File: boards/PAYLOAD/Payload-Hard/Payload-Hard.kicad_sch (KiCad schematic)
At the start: 18 parts, among them J101 Micro_SD_Card, J102 Conn_01x05_Female, J103 Conn_01x07_Male, P101 S3B-PH-SM4-TB, U1 LM358, U102 3SP_SO2_20

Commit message: Yo
Yo
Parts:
- removed U1: LM358, Package_DIP:DIP-8_W10.16mm, symbol Amplifier_Operational:LM358
- added J104: Screw_Terminal_01x02, TerminalBlock_TE-Connectivity:TerminalBlock_TE_282834-2_1x02_P2.54mm_Horizontal, symbol Connector:Screw_Terminal_01x02
- added U101: OPAMP, symbol pspice:OPAMP
- added U103: Opamp_Dual, symbol Device:Opamp_Dual
- R108: value 10k -> R_US
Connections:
- net 3V3: now also U101.4 (V+)
- net Counter: now also U101.3
- net GND: now also J104.2 (Pin_2), U101.5 (V-)
- net Reference: now also U101.2 (-)
- net SO2_Out: now also U103.1
- net at R101.2, R102.1: now also U101.1 (+)
- net at C103.1, R106.2, R108.1: now also U103.2 (-)
- net at R105.2, R107.1: now also U103.3 (+)
- net Vbattery: now reaches A101.30 (VIN)
- net Vbattery: now also J104.1 (Pin_1)
- no-connect marks 19 -> 18
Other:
- note added: "Power Pins"

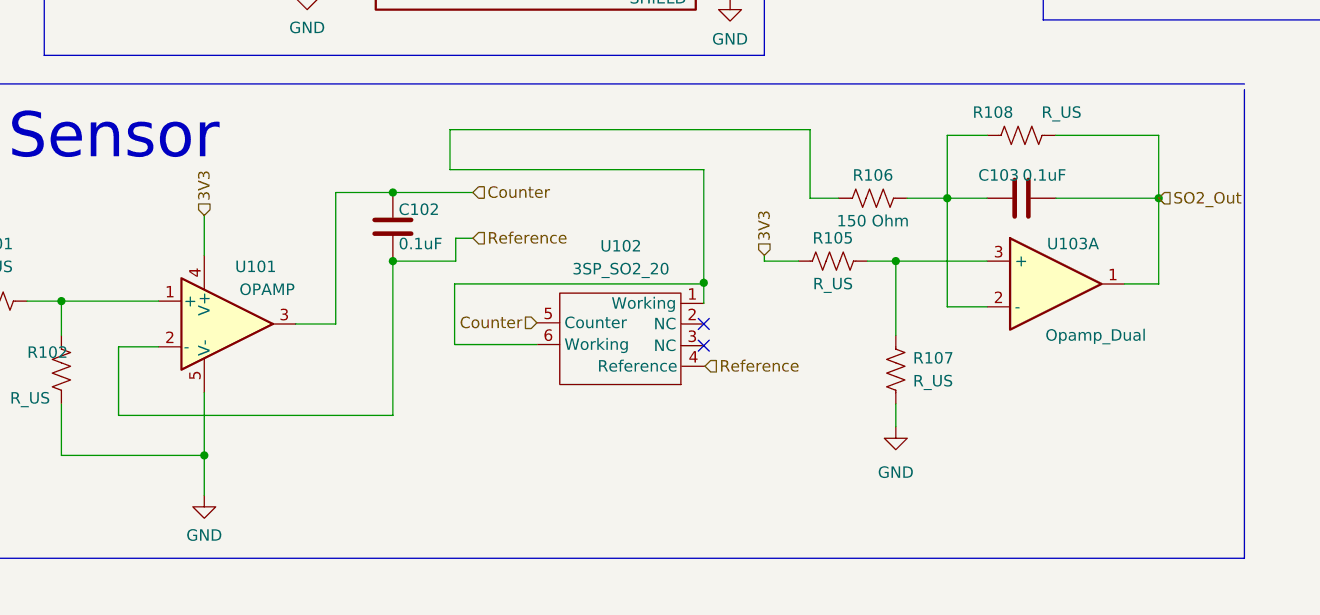
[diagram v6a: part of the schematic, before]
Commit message: CHanged OpAmp Symbol
CHanged OpAmp Symbol
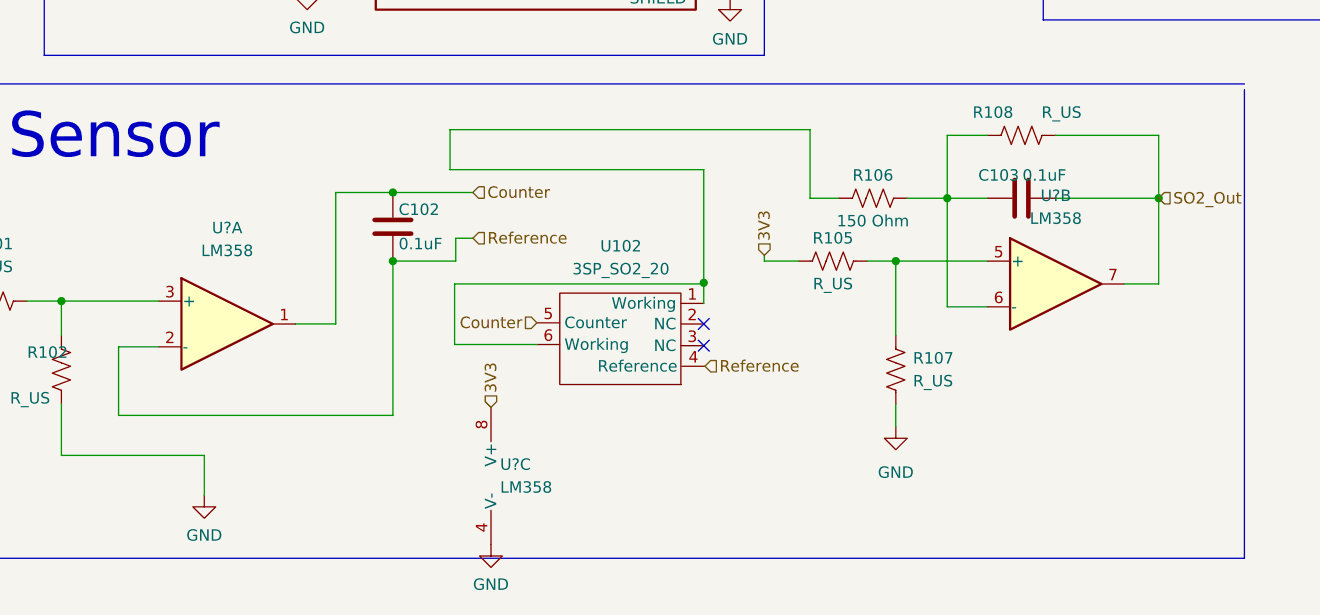
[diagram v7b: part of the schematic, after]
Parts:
- removed U101: OPAMP, symbol pspice:OPAMP
- removed U103: Opamp_Dual, symbol Device:Opamp_Dual
- added U? (x2): LM358, symbol Amplifier_Operational:LM358
- added U?: LM358, Package_DIP:DIP-8_W10.16mm, symbol Amplifier_Operational:LM358
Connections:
- net 3V3: now also U?.8 (V+)
- net Counter: now also U?.1
- net GND: now also U?.4 (V-)
- net Reference: now also U?.2 (-)
- net SO2_Out: now also U?.7
- net at C103.1, R106.2, R108.1: now also U?.6 (-)
- net at R105.2, R107.1: now also U?.5 (+)
- net at R101.2, R102.1: now also U?.3 (+)

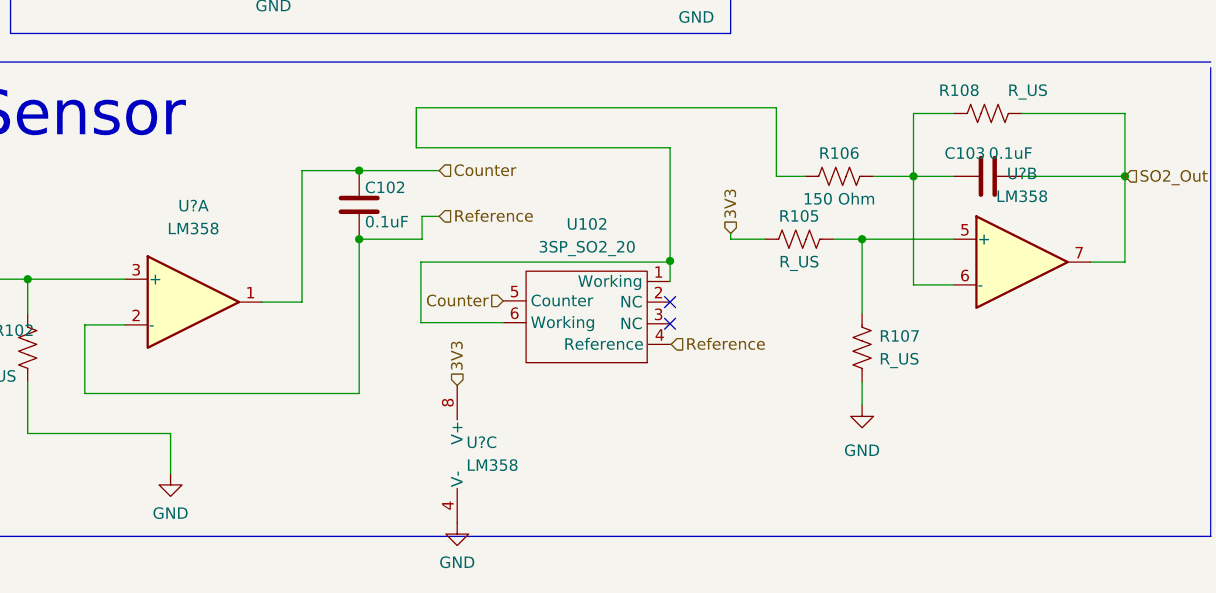
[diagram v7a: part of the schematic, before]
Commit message: New Schematic Title
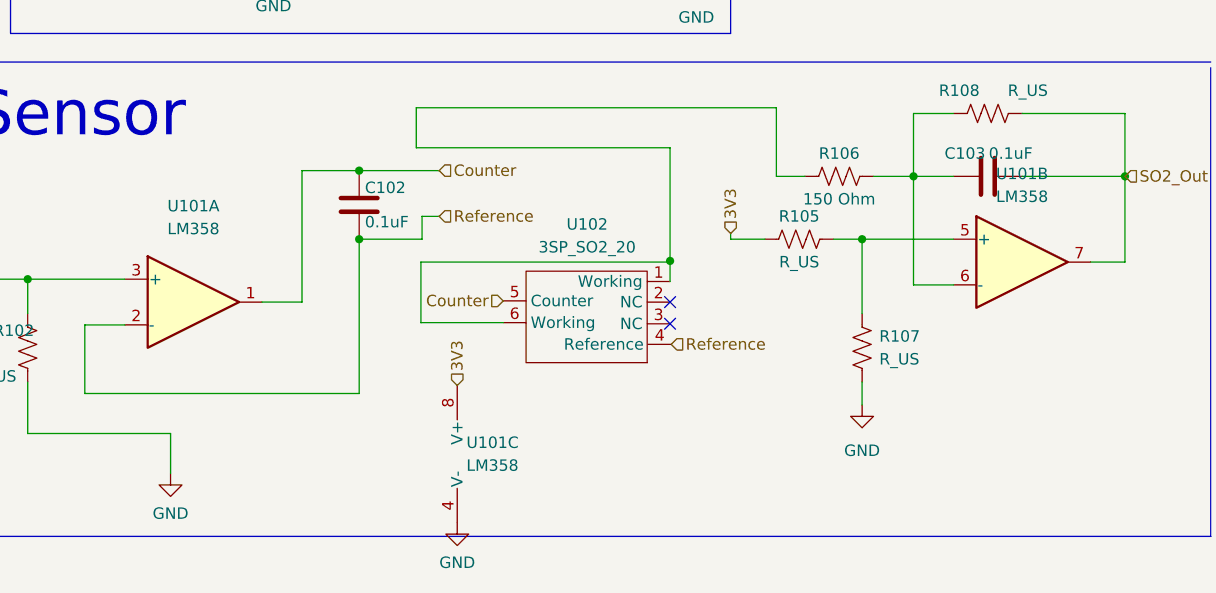
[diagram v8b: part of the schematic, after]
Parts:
- gave numbers to parts that had none: 1
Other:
- company: (none) -> Illinois Space Society
- title: My Dick is Hard 4 U -> Payload Hard
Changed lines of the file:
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@@
   (paper "A4")
   (title_block
-    (title "My Dick is Hard 4 U")
+    (title "Payload Hard")
+    (date "05/30/22")
+    (rev "V1")
+    (company "Illinois Space Society")
+    (comment 1 "Philip Zolfaghari")
+    (comment 2 "Rishi Gottumukkala")
   )
   (junction (at 165.735 144.78) (diameter 0) (color 0 0 0 0)
@@
   (symbol (lib_id "Amplifier_Operational:LM358") (at 94.0816 175.641 0) (unit 3)
     (in_bom yes) (on_board yes) (fields_autoplaced)
-    (property "Reference" "U?" (id 0) (at 92.5576 174.3709 0)
+    (property "Reference" "U101" (id 0) (at 92.5576 174.3709 0)
       (effects (font (size 1.27 1.27)) (justify left))
     )
@@
   (symbol (lib_id "Amplifier_Operational:LM358") (at 62.23 158.75 0) (unit 1)
     (in_bom yes) (on_board yes) (fields_autoplaced)
-    (property "Reference" "U?" (id 0) (at 62.23 148.082 0))
+    (property "Reference" "U101" (id 0) (at 62.23 148.082 0))
     (property "Value" "LM358" (id 1) (at 62.23 150.622 0))
     (property "Footprint" "Package_DIP:DIP-8_W10.16mm" (id 2) (at 62.23 158.75 0)
@@
   (symbol (lib_id "Amplifier_Operational:LM358") (at 154.305 154.305 0) (unit 2)
     (in_bom yes) (on_board yes) (fields_autoplaced)
-    (property "Reference" "U?" (id 0) (at 154.305 144.5006 0))
+    (property "Reference" "U101" (id 0) (at 154.305 144.5006 0))
     (property "Value" "LM358" (id 1) (at 154.305 147.0406 0))
     (property "Footprint" "" (id 2) (at 154.305 154.305 0)
@@
   (symbol (lib_id "power:GND") (at 91.5416 183.261 0) (unit 1)
     (in_bom yes) (on_board yes)
-    (property "Reference" "#PWR?" (id 0) (at 91.5416 189.611 0)
+    (property "Reference" "#PWR0110" (id 0) (at 91.5416 189.611 0)
       (effects (font (size 1.27 1.27)) hide)
     )
@@
     )
     (path "/77661e9b-b852-4519-ba11-9b41a5d8adac"
-      (reference "#PWR?") (unit 1) (value "GND") (footprint "")
+      (reference "#PWR0110") (unit 1) (value "GND") (footprint "")
     )
     (path "/a91a09ae-7da8-46f5-893f-cfe40ca8737a"
@@
       (reference "R108") (unit 1) (value "R_US") (footprint "Resistor_SMD:R_0805_2012Metric")
     )
+    (path "/51ad441d-8209-4491-b8fb-dbe0a29eee44"
+      (reference "U101") (unit 1) (value "LM358") (footprint "Package_DIP:DIP-8_W10.16mm")
+    )
+    (path "/53bc31ee-b669-4dc2-81f5-0e8bb0051201"
+      (reference "U101") (unit 2) (value "LM358") (footprint "")
+    )
+    (path "/4f80ff6d-df41-4992-ba86-f12541220d37"
+      (reference "U101") (unit 3) (value "LM358") (footprint "")
+    )
     (path "/325b982e-7665-4281-8762-9f7b5f3809a1"
       (reference "U102") (unit 1) (value "3SP_SO2_20") (footprint "Sensor:3SP_SO2_20")
     )
-    (path "/51ad441d-8209-4491-b8fb-dbe0a29eee44"
-      (reference "U?") (unit 1) (value "LM358") (footprint "Package_DIP:DIP-8_W10.16mm")
-    )
-    (path "/53bc31ee-b669-4dc2-81f5-0e8bb0051201"
-      (reference "U?") (unit 2) (value "LM358") (footprint "")
-    )
-    (path "/4f80ff6d-df41-4992-ba86-f12541220d37"
-      (reference "U?") (unit 3) (value "LM358") (footprint "")
-    )
-  )
+  )
